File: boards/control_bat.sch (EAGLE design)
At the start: 12 parts, among them U1 MCP1703T-3002E/CB, U3 LPC824M201JDH20J, X2 53398-04

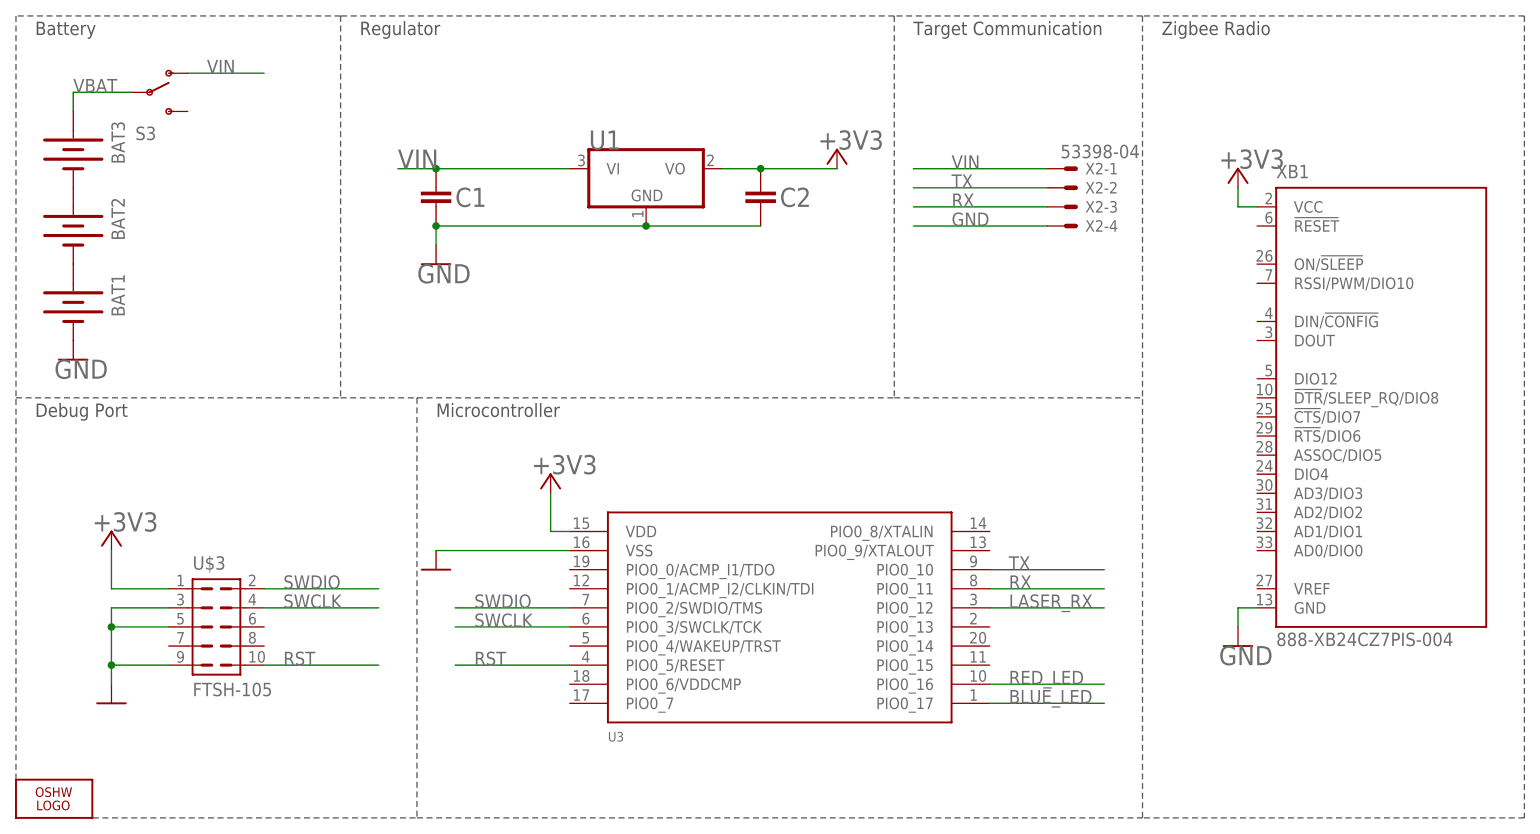
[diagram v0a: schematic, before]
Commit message: First pass layout of control/battery board
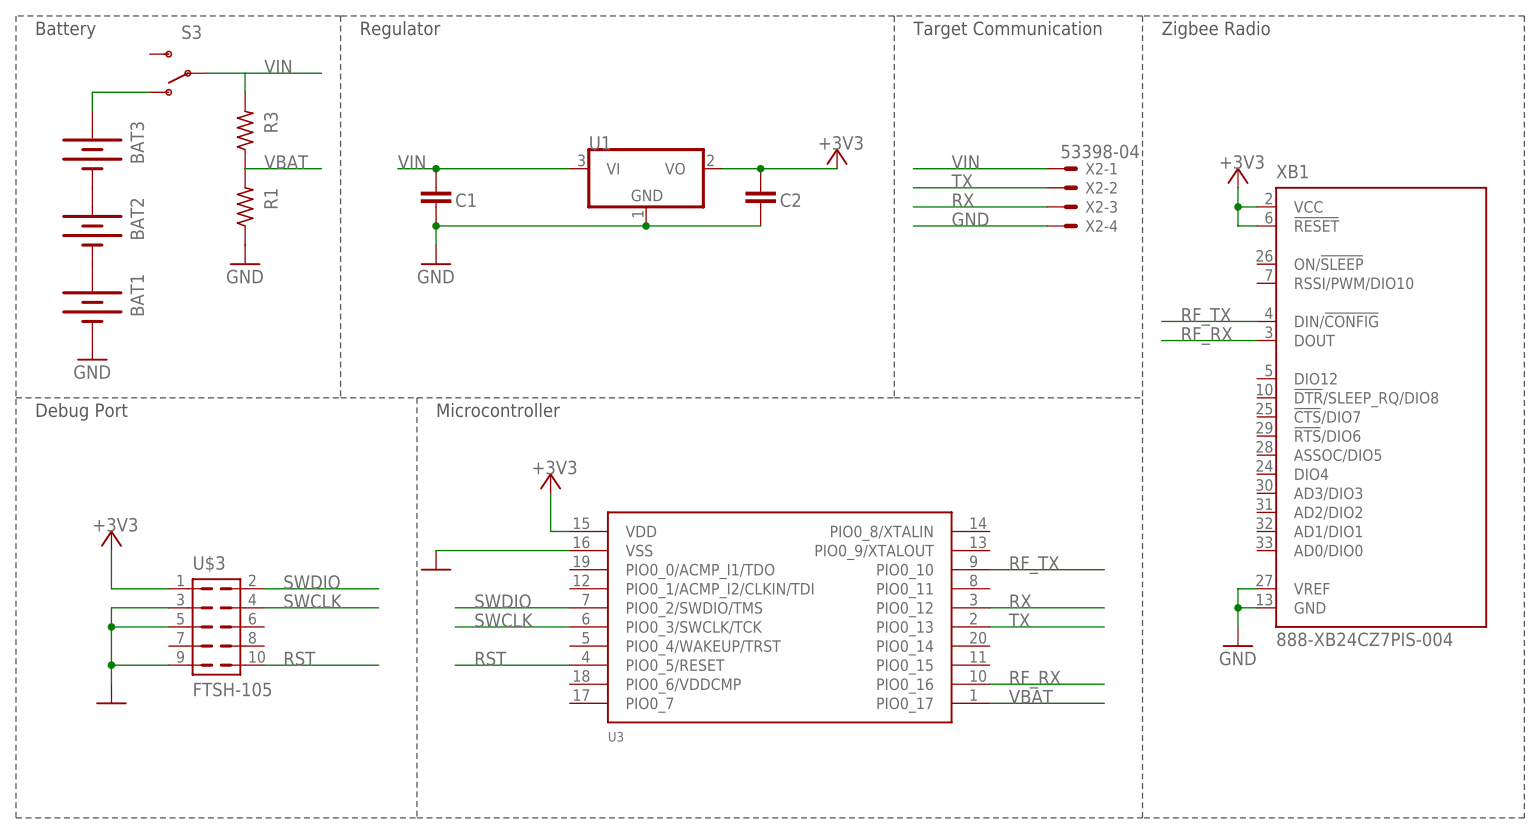
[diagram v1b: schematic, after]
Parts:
- removed LOGO2: OSHW_LOGO_FILLX0150-NT, ohw-logo:OSHW_LOGO_FILLX0150-NT
- added R1, R3: 10k, rcl:R-US_R0603
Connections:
- removed net BLUE_LED: U3.PIO0_17
- removed net LASER_RX: U3.PIO0_12
- removed net RED_LED: U3.PIO0_16
- new net N$3: BAT3.+, S3.O
- new net RF_RX: U3.PIO0_16, XB1.DOUT
- new net RF_TX: U3.PIO0_10, XB1.DIN/!CONFIG
- net +3V3: now also XB1.!RESET
- net GND: now also R1.1, XB1.VREF
- net RX: now also U3.PIO0_12; no longer U3.PIO0_11
- net TX: now also U3.PIO0_13; no longer U3.PIO0_10
- net VBAT: now also R1.2, R3.1, U3.PIO0_17; no longer BAT3.+, S3.P
- net VIN: now also R3.2, S3.P; no longer S3.O
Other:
- moved on the sheet: BAT1, BAT2, BAT3, S3

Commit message: Add serial debug port on xbee in case I need to configure it manually
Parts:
- added JP1: (no value), SparkFun-Connectors:M03PTH
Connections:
- net RF_RX: now also JP1.1
- net RF_TX: now also JP1.2
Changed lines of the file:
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@@
 <part name="R1" library="rcl" deviceset="R-US_" device="R0603" value="10k"/>
 <part name="GND1" library="supply1" deviceset="GND" device=""/>
+<part name="JP1" library="SparkFun-Connectors" deviceset="M03" device="PTH"/>
+<part name="GND6" library="supply1" deviceset="GND" device=""/>
 </parts>
 <sheets>
@@
 <attribute name="VALUE" x="241.3" y="73.66" size="1.778" layer="96"/>
 </instance>
+<instance part="JP1" gate="G$1" x="396.24" y="12.7" rot="R180"/>
+<instance part="GND6" gate="1" x="386.08" y="7.62" smashed="yes">
+<attribute name="VALUE" x="383.54" y="5.08" size="1.778" layer="96"/>
+</instance>
 </instances>
 <busses>
@@
 <label x="345.44" y="35.56" size="1.778" layer="95"/>
 </segment>
+<segment>
+<pinref part="JP1" gate="G$1" pin="2"/>
+<wire x1="388.62" y1="12.7" x2="375.92" y2="12.7" width="0.1524" layer="91"/>
+<label x="378.46" y="12.7" size="1.778" layer="95"/>
+</segment>
 </net>
 <net name="RF_RX" class="0">
@@
 <label x="345.44" y="20.32" size="1.778" layer="95"/>
 </segment>
-</net>
+<segment>
+<pinref part="JP1" gate="G$1" pin="1"/>
+<wire x1="388.62" y1="15.24" x2="375.92" y2="15.24" width="0.1524" layer="91"/>
+<label x="378.46" y="15.24" size="1.778" layer="95"/>
+</segment>
+</net>

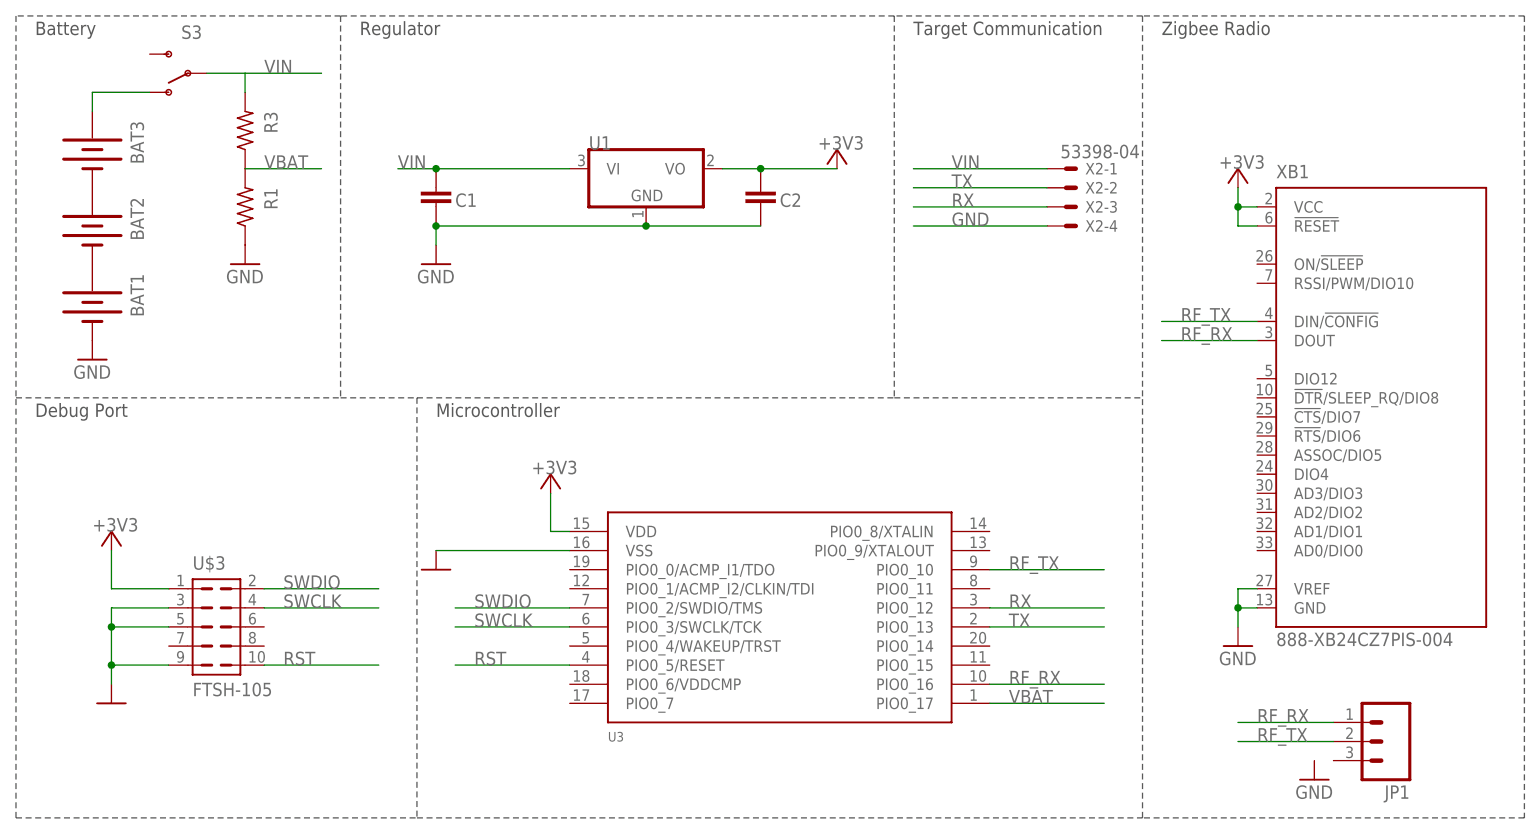
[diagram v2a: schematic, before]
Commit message: Fix footprint (was footprint for LPC812 instead of LPC824). Update part numbers on the schematic. Add IR. Cleanup ground plane.
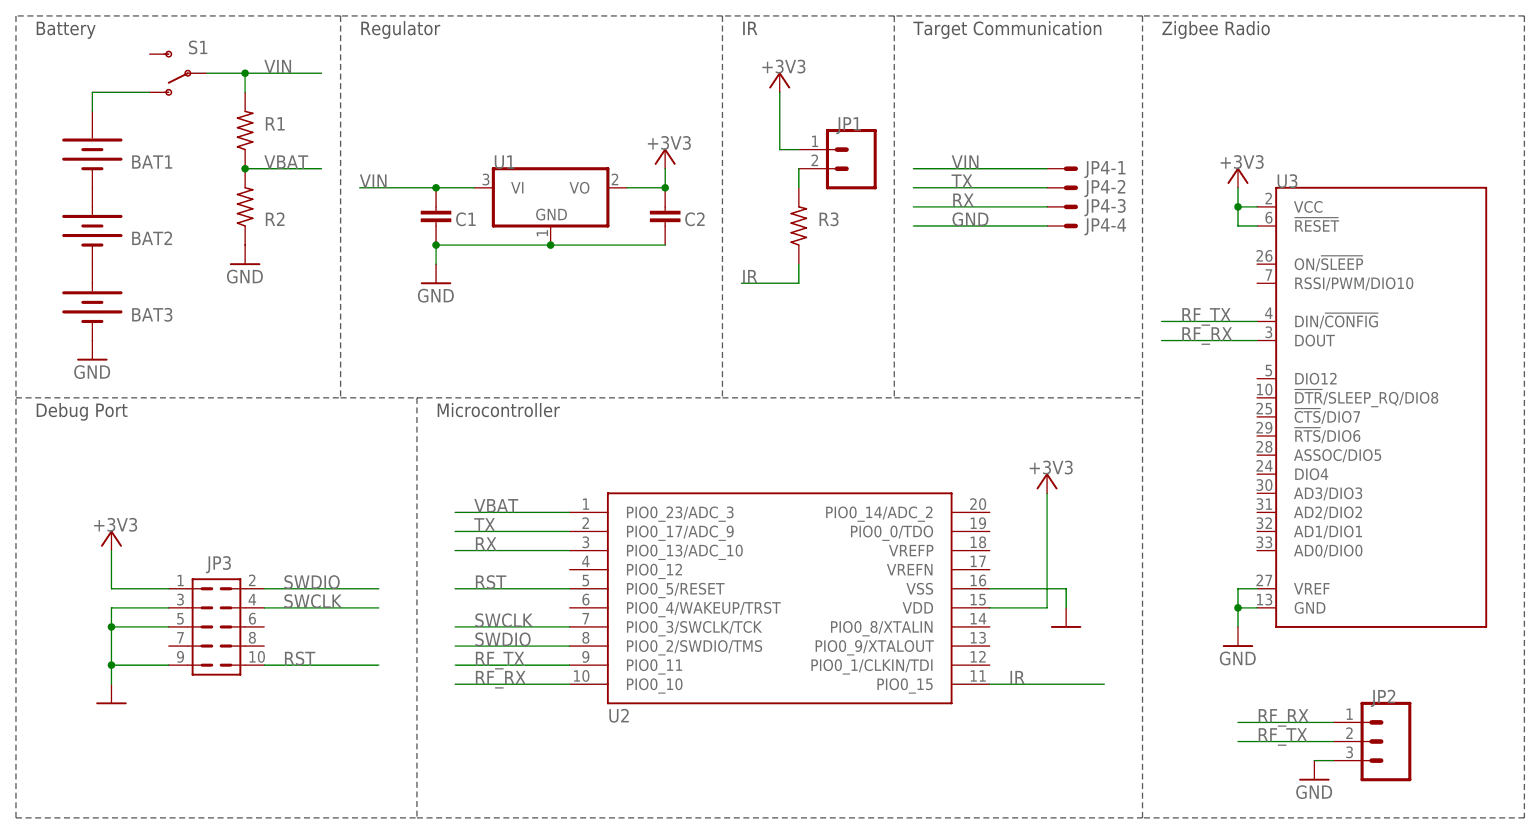
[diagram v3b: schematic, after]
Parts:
- removed XB1: 888-XB24CZ7PIS-004, xbee:XBEE-SMT
- added JP2: (no value), SparkFun-Connectors:M03PTH
- added R2: 71-CRCW0603-10K-E3, rcl:R-US_R0603
- added U2: 771-LPC824M201JDH20J, torpedo:LPC824
- JP1: value (none) -> M02PTH; device SparkFun-Connectors:M03PTH -> SparkFun-Connectors:M02PTH
- JP3: value FTSH-105 -> FTSH-105-01-L
- JP4: value 53398-04 -> 798-DF134P125V20
- R1: value 10k -> 71-CRCW0603-10K-E3
- R3: value 10k -> 71-CRCW0603220RFKEB
- S1: value (none) -> 612-EG1270
- U1: value MCP1703T-3002E/CB -> 579-MCP1703T-3002ECB
- U3: value LPC824M201JDH20J -> 888-XB24CZ7PIS-004; device LPC800:LPC812M101JDH20 -> xbee:XBEE-SMT
- renumbered S3 to S1, U$3 to JP3, X2 to JP4
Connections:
- new net IR: R3.1, U2.PIO0_15
- new net N$4: JP1.2, R3.2
- net +3V3: now also JP1.1, U2.VDD, U3.!RESET, U3.VCC; no longer U3.VDD, XB1.!RESET, XB1.VCC
- net GND: now also BAT3.-, JP2.3, R2.1, U2.VSS, U3.GND, U3.VREF; no longer BAT1.-, R1.1, U3.VSS, XB1.GND, XB1.VREF
- net N$1: now also BAT3.+; no longer BAT1.+
- net N$2: now also BAT1.-; no longer BAT3.-
- net N$3: now also BAT1.+; no longer BAT3.+
- net RF_RX: now also JP2.1, U2.PIO0_10, U3.DOUT; no longer JP1.1, U3.PIO0_16, XB1.DOUT
- net RF_TX: now also JP2.2, U2.PIO0_11, U3.DIN/!CONFIG; no longer JP1.2, U3.PIO0_10, XB1.DIN/!CONFIG
- net RST: now also U2.PIO0_5/RESET; no longer U3.PIO0_5/RESET
- net RX: now also U2.PIO0_13/ADC_10; no longer U3.PIO0_12
- net SWCLK: now also U2.PIO0_3/SWCLK/TCK; no longer U3.PIO0_3/SWCLK/TCK
- net SWDIO: now also U2.PIO0_2/SWDIO/TMS; no longer U3.PIO0_2/SWDIO/TMS
- net TX: now also U2.PIO0_17/ADC_9; no longer U3.PIO0_13
- net VBAT: now also R1.1, R2.2, U2.PIO0_23/ADC_3; no longer R1.2, R3.1, U3.PIO0_17
- net VIN: now also R1.2; no longer R3.2
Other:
- note added: "IR"
- moved on the sheet: BAT1, BAT3, C1, C2, R1, R3, U1

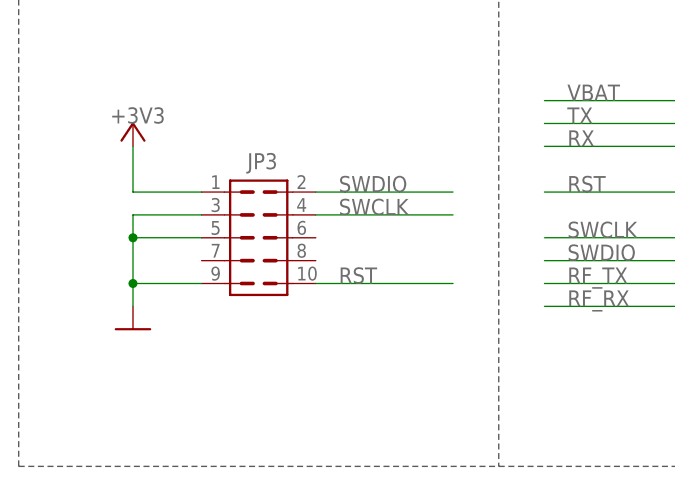
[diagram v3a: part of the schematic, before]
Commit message: Probably not a bad idea to have a pullup on the reset line.
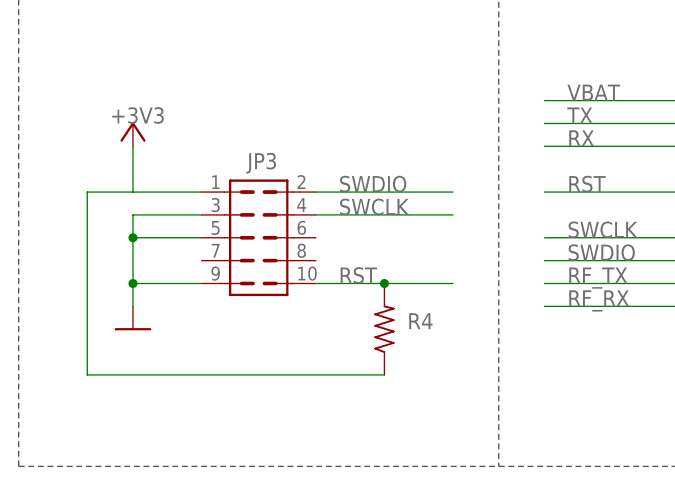
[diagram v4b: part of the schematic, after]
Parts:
- added R4: 71-CRCW0603-10K-E3, rcl:R-US_R0603
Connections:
- net +3V3: now also R4.1
- net RST: now also R4.2
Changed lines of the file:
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@@
 <setting verticaltext="up"/>
 </settings>
-<grid distance="0.1" unitdist="inch" unit="inch" style="lines" multiple="1" display="yes" altdistance="0.01" altunitdist="inch" altunit="inch"/>
+<grid distance="0.1" unitdist="inch" unit="inch" style="lines" multiple="1" display="no" altdistance="0.01" altunitdist="inch" altunit="inch"/>
 <layers>
 <layer number="1" name="Top" color="4" fill="1" visible="no" active="no"/>
@@
 <part name="+3V34" library="supply1" deviceset="+3V3" device=""/>
 <part name="GND5" library="supply1" deviceset="GND" device=""/>
+<part name="R4" library="rcl" deviceset="R-US_" device="R0603" value="71-CRCW0603-10K-E3"/>
 </parts>
 <sheets>
@@
 </instance>
 <instance part="GND5" gate="1" x="353.06" y="27.94" smashed="yes"/>
+<instance part="R4" gate="G$1" x="254" y="17.78" smashed="yes" rot="R90">
+<attribute name="NAME" x="256.54" y="17.78" size="1.778" layer="95"/>
+</instance>
 </instances>
 <busses>
@@
 <wire x1="233.68" y1="33.02" x2="226.06" y2="33.02" width="0.1524" layer="91"/>
 <wire x1="226.06" y1="33.02" x2="226.06" y2="38.1" width="0.1524" layer="91"/>
+<wire x1="226.06" y1="33.02" x2="220.98" y2="33.02" width="0.1524" layer="91"/>
+<wire x1="220.98" y1="33.02" x2="220.98" y2="12.7" width="0.1524" layer="91"/>
+<pinref part="R4" gate="G$1" pin="1"/>
+<wire x1="220.98" y1="12.7" x2="254" y2="12.7" width="0.1524" layer="91"/>
 </segment>
 <segment>
@@
 <segment>
 <pinref part="JP3" gate="G$1" pin="10"/>
-<wire x1="246.38" y1="22.86" x2="261.62" y2="22.86" width="0.1524" layer="91"/>
+<wire x1="246.38" y1="22.86" x2="254" y2="22.86" width="0.1524" layer="91"/>
 <label x="248.92" y="22.86" size="1.778" layer="95"/>
-</segment>
-<segment>
+<pinref part="R4" gate="G$1" pin="2"/>
+<wire x1="254" y1="22.86" x2="261.62" y2="22.86" width="0.1524" layer="91"/>
+<junction x="254" y="22.86"/>
+</segment>
+<segment>
